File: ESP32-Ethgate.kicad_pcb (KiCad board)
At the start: 2 copper layers, 71.2 x 38.1 mm, 54 parts, among them J1 USB_B_Micro, J2 HR911105A, Q1 UMH3N, U1 HT7233, U2 ESP32-WROOM-32U, U3 CH340C, U4 HT7233, U5 LAN8720A, U6 USBLC6-2SC6

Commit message: more tuning
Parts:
- D4: value GREEN -> RED
- moved FB1 2.85 mm to (93.5, 77.2), turned to 180 degrees
- moved C14 1.96 mm to (93.5, 80.5), turned to 0 degrees
- moved C17 0.65 mm to (93.5, 78.9), turned to 0 degrees
- moved C10 0.47 mm to (97.5, 80.9)
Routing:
- net /+3V3_LAN: track 47.8 -> 49.8 mm
- net GND: track 56.6 -> 54.7 mm, vias 52 -> 55
- net +3.3VA: track 105.9 -> 107.1 mm
- net +3V3: vias 9 -> 8
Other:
- net class Power: via_dia 1.5 -> 1.2; via_drill 0.9 -> 0.6

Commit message: PDF schematic
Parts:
- moved R15 20.8 mm to (123.8, 93.5), turned to 90 degrees
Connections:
- net /RXN renamed /RX-
- net /RXP renamed /RX+
- net /TXN renamed /TX-
- net /TXP renamed /TX+
- J1 pad 4: (no net) -> unconnected-(J1-Pad4)
- U2 pad 13: (no net) -> unconnected-(U2-Pad13)
- U2 pad 16: (no net) -> unconnected-(U2-Pad16)
- U2 pad 17: (no net) -> unconnected-(U2-Pad17)
- U2 pad 18: (no net) -> unconnected-(U2-Pad18)
- U2 pad 19: (no net) -> unconnected-(U2-Pad19)
- U2 pad 20: (no net) -> unconnected-(U2-Pad20)
- U2 pad 21: (no net) -> unconnected-(U2-Pad21)
- U2 pad 22: (no net) -> unconnected-(U2-Pad22)
- U2 pad 23: (no net) -> unconnected-(U2-Pad23)
- U2 pad 26: (no net) -> unconnected-(U2-Pad26)
- U2 pad 27: (no net) -> unconnected-(U2-Pad27)
- U2 pad 29: (no net) -> unconnected-(U2-Pad29)
- U2 pad 32: (no net) -> unconnected-(U2-Pad32)
- U2 pad 4: (no net) -> unconnected-(U2-Pad4)
- U2 pad 5: (no net) -> unconnected-(U2-Pad5)
- U2 pad 6: (no net) -> unconnected-(U2-Pad6)
- U2 pad 7: (no net) -> unconnected-(U2-Pad7)
- U2 pad 8: (no net) -> unconnected-(U2-Pad8)
- U2 pad 9: (no net) -> unconnected-(U2-Pad9)
- U3 pad 10: (no net) -> unconnected-(U3-Pad10)
- U3 pad 11: (no net) -> unconnected-(U3-Pad11)
- U3 pad 12: (no net) -> unconnected-(U3-Pad12)
- U3 pad 15: (no net) -> unconnected-(U3-Pad15)
- U3 pad 7: (no net) -> unconnected-(U3-Pad7)
- U3 pad 8: (no net) -> unconnected-(U3-Pad8)
- U3 pad 9: (no net) -> unconnected-(U3-Pad9)
- U5 pad 14: (no net) -> unconnected-(U5-Pad14)
- U5 pad 4: (no net) -> unconnected-(U5-Pad4)
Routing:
- net /XTAL: track 4.53 -> 44.6 mm
- net /PHY_CLK: track 27.1 -> 4.20 mm
- net /RXD1: track 30.5 -> 42.1 mm
- net /RXD0: track 30.5 -> 40.3 mm
- net /RX-: track 17.5 -> 23.6 mm
- net /TX-: track 17.9 -> 21.2 mm
- net /TXD1: track 51.1 -> 48.3 mm
- net /TX+: track 20.5 -> 21.6 mm
- net /MDIO: track 32.1 -> 32.9 mm
- net /RX+: track 24.5 -> 23.9 mm
- net GND1: vias 13 -> 14
- net GND: vias 55 -> 56
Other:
- net class Default removed
- net class Power removed

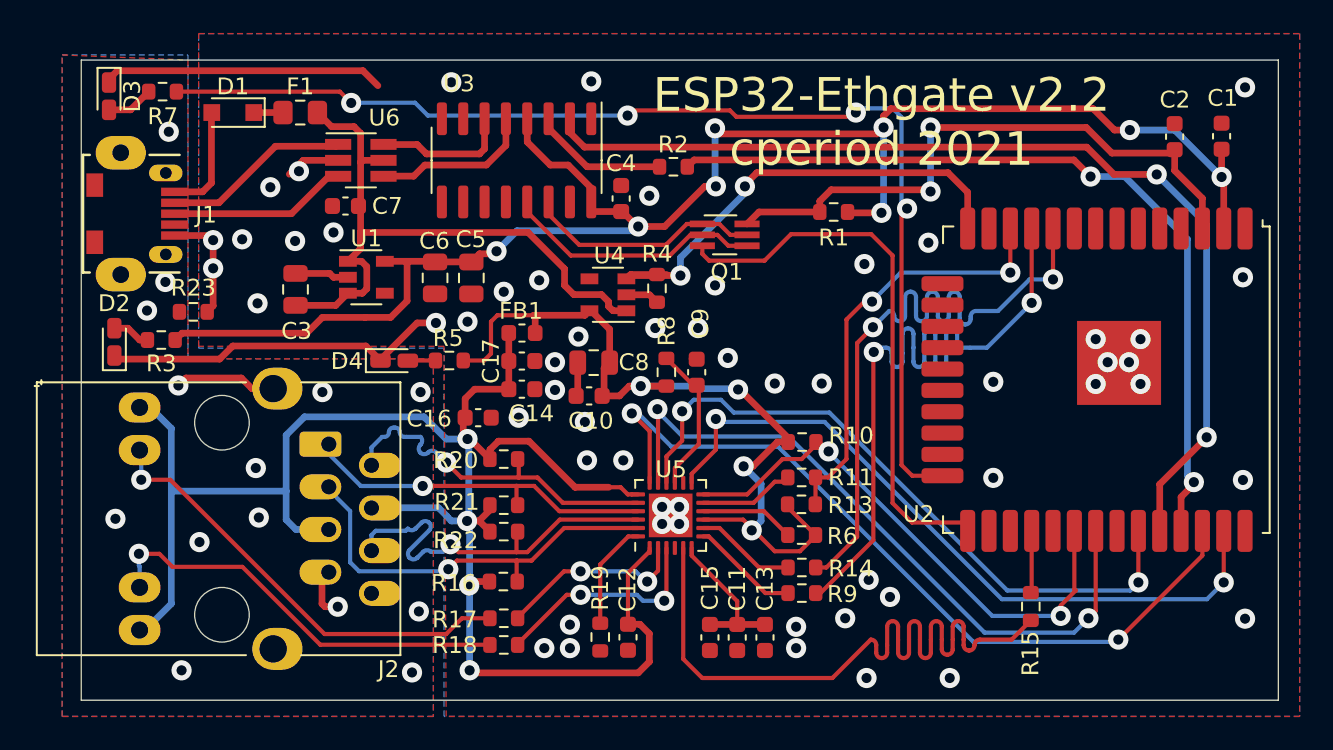
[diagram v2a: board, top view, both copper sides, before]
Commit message: update Kicad
make sure REGOFF is properly pulled low, fixing #1

add some 1.25mm pitch connectors for USB and a couple of GPIO's

Assorted tweaks to some routing to ensure RMII signals and the clock are
somewhat length matched.

Extend the ground exclusion zone to past where the eth magnetics should
be found.
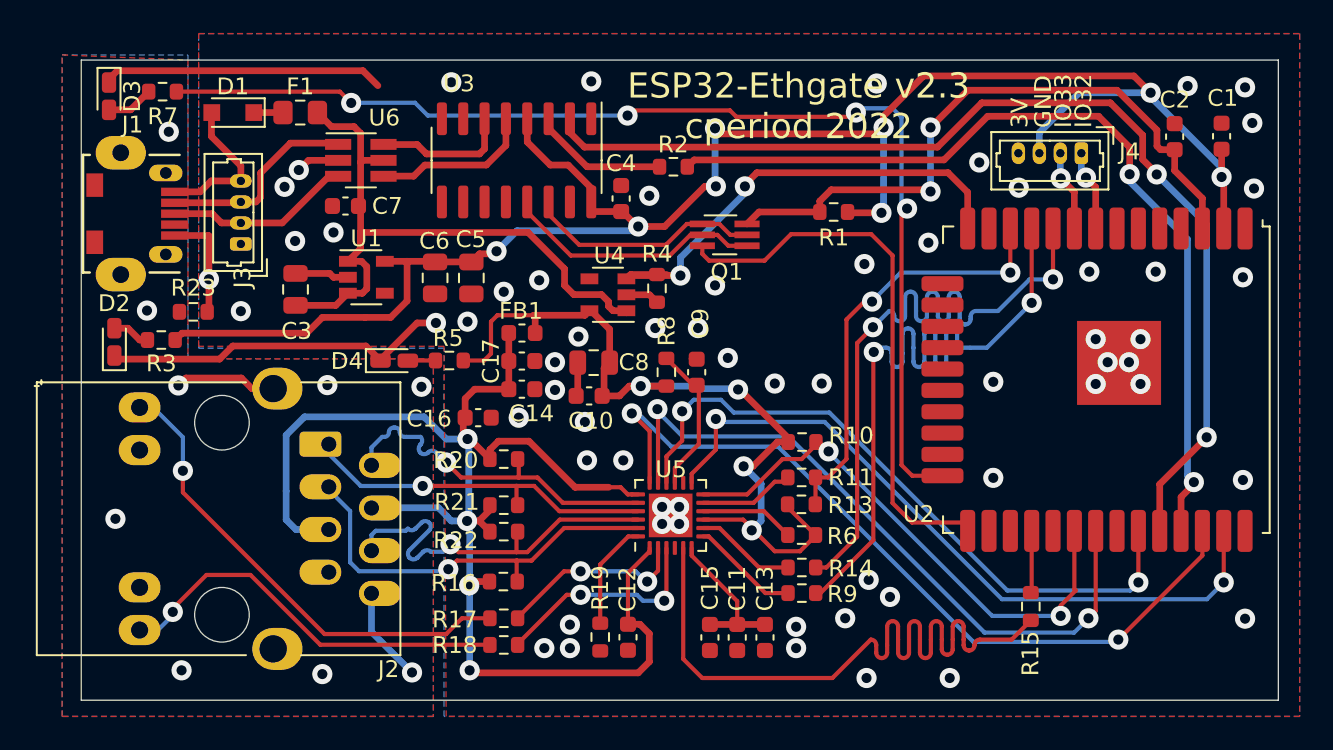
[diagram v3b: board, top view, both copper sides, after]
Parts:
- added J3: USB, Connector_Molex:Molex_PicoBlade_53047-0410_1x04_P1.25mm_Vertical, F.Cu at (76.8, 71.9)
- added J4: GPIO, Connector_Molex:Molex_PicoBlade_53047-0410_1x04_P1.25mm_Vertical, F.Cu at (126.8, 66.5)
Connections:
- net Net-(D1-Pad2) renamed /VBUS
- net Net-(J1-Pad2) renamed /DM
- net Net-(J1-Pad3) renamed /DP
- J2 pad 10: Net-(J2-Pad10) -> GND1
- J2 pad 11: Net-(J2-Pad11) -> GND1
- J2 pad 12: +3.3VA -> Net-(J2-Pad12)
- J2 pad 7: GND1 -> unconnected-(J2-Pad7)
- J2 pad 9: +3.3VA -> Net-(J2-Pad9)
- R17 pad 2: Net-(J2-Pad10) -> Net-(J2-Pad9)
- R18 pad 2: Net-(J2-Pad11) -> Net-(J2-Pad12)
- U2 pad 6: unconnected-(U2-Pad6) -> /IO34
- U2 pad 7: unconnected-(U2-Pad7) -> /IO35
- U2 pad 8: unconnected-(U2-Pad8) -> /IO32
- U2 pad 9: unconnected-(U2-Pad9) -> /IO33
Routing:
- net Net-(J2-Pad9): track 0.00 -> 28.8 mm, vias 0 -> 1
- net Net-(J2-Pad10): track 26.8 -> 0.00 mm, vias 1 -> 0
- net Net-(J2-Pad11): track 25.2 -> 0.00 mm, vias 1 -> 0
- net Net-(J2-Pad12): track 0.00 -> 24.2 mm, vias 0 -> 1
- net +3.3VA: track 107.1 -> 84.9 mm
- net +3V3: track 99.2 -> 110.1 mm
- net /IO32: track 0.00 -> 5.33 mm, vias 0 -> 1
- net /IO33: track 0.00 -> 5.32 mm, vias 0 -> 1
- net /eTX: track 49.4 -> 52.7 mm
- net /eRX: track 59.9 -> 62.9 mm
- net GND1: track 9.15 -> 11.8 mm, vias 14 -> 9
- net /VBUS: track 6.62 -> 9.02 mm
- net /EN: track 37.1 -> 39.3 mm
- net /DM: track 11.2 -> 12.1 mm
- net GND: track 54.7 -> 53.8 mm, vias 56 -> 62
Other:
- board text added: "3V"
- board text added: "ESP32-Ethgate v2.3 cperiod 2022"
- board text added: "GND"
- board text added: "IO32"
- board text added: "IO33"
- board text removed: "ESP32-Ethgate v2.2 cperiod 2021"

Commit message: update the various extra files
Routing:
- net +3V3: track 110.1 -> 113.5 mm, vias 8 -> 7
- net Net-(J2-Pad12): track 24.2 -> 23.1 mm
- net +3.3VA: track 84.9 -> 84.0 mm
- net /+3V3_LAN: track 49.8 -> 49.0 mm
- net Net-(J2-Pad9): track 28.8 -> 27.9 mm
- net RTS: track 14.1 -> 13.3 mm
- net /TX+: track 21.6 -> 20.9 mm
- net DTR: track 15.5 -> 14.9 mm
- net Net-(R2-Pad2): track 8.12 -> 7.55 mm
- net /DP: track 11.1 -> 10.6 mm

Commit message: label the USB connections
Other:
- board text added: "5V"
- board text added: "D+"
- board text added: "D-"
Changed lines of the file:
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@@
       (effects (font (size 1 1) (thickness 0.15)))
     )
-    (fp_text value "USB" (at 1.88 2.35 90) (layer "F.Fab")
+    (fp_text value "USB" (at 5.9668 -0.0736 180) (layer "F.Fab")
       (effects (font (size 1 1) (thickness 0.15)))
     )
@@
     (effects (font (size 1.5 1.5) (thickness 0.2)))
   )
+  (gr_text "D+" (at 78.0542 70.6628) (layer "F.SilkS")
+    (effects (font (size 1 1) (thickness 0.15)) (justify left))
+  )
   (gr_text "GND" (at 124.557 65.0052 90) (layer "F.SilkS")
     (effects (font (size 1 1) (thickness 0.15)) (justify left))
@@
     (effects (font (size 1 1) (thickness 0.15)) (justify left))
   )
+  (gr_text "5V" (at 78.0542 68.1228) (layer "F.SilkS")
+    (effects (font (size 1 1) (thickness 0.15)) (justify left))
+  )
+  (gr_text "D-" (at 78.0542 69.3928) (layer "F.SilkS")
+    (effects (font (size 1 1) (thickness 0.15)) (justify left))
+  )
+  (gr_text "GND" (at 78.0542 71.9328) (layer "F.SilkS")
+    (effects (font (size 1 1) (thickness 0.15)) (justify left))
+  )

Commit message: properly fix the nINTSEL for #1 (and document the bootstrap settings in the schematic so I remember next time).
this implicitly updates to Kicad 7.
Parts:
- turned R17 to 0 degrees
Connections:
- J2 pad 10: GND1 -> Net-(J2-Pad10)
- J2 pad 9: Net-(J2-Pad9) -> +3.3VA
- R17 pad 1: /LINKLED -> Net-(J2-Pad10)
- R17 pad 2: Net-(J2-Pad9) -> /LINKLED
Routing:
- net Net-(J2-Pad9): track 27.9 -> 0.00 mm, vias 1 -> 0
- net Net-(J2-Pad10): track 0.00 -> 27.2 mm, vias 0 -> 1
- net +3.3VA: track 84.0 -> 94.0 mm

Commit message: update rev number
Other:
- board text added: "ESP32-Ethgate v2.4 cperiod 2022"
- board text removed: "ESP32-Ethgate v2.3 cperiod 2022"
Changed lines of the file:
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@@
   (gr_line (start 67.31 60.96) (end 67.31 99.06)
     (stroke (width 0.05) (type solid)) (layer "Edge.Cuts"))
-  (gr_text "ESP32-Ethgate v2.3\ncperiod 2022" (at 110.007 63.7052) (layer "F.SilkS")
+  (gr_text "ESP32-Ethgate v2.4\ncperiod 2022" (at 110.007 63.7052) (layer "F.SilkS")
     (effects (font (size 1.5 1.5) (thickness 0.2)))
   )
